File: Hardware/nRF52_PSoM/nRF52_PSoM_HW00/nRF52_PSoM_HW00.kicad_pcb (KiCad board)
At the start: 4 copper layers, 22 x 25.6 mm, 54 parts, among them J101 USB4510-03-1-A, J102 54722-0604, SW401 SW_Push, SW402 SW_Push, U201 BQ24075RGTR, U301 MIC5528-3.3YMT-T5, U401 ESP32-S2FH4, Y601 Crystal_GND24_Small

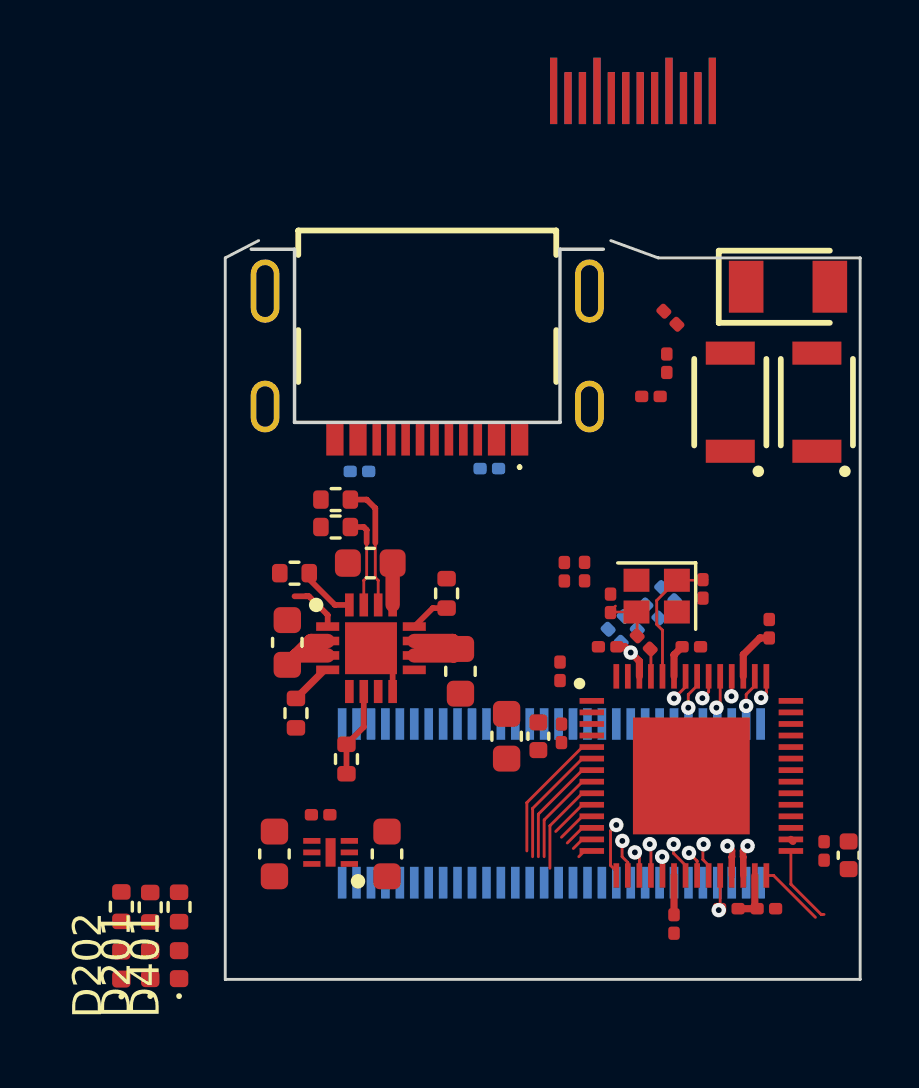
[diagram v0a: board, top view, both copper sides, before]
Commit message: Routing ESP32S2
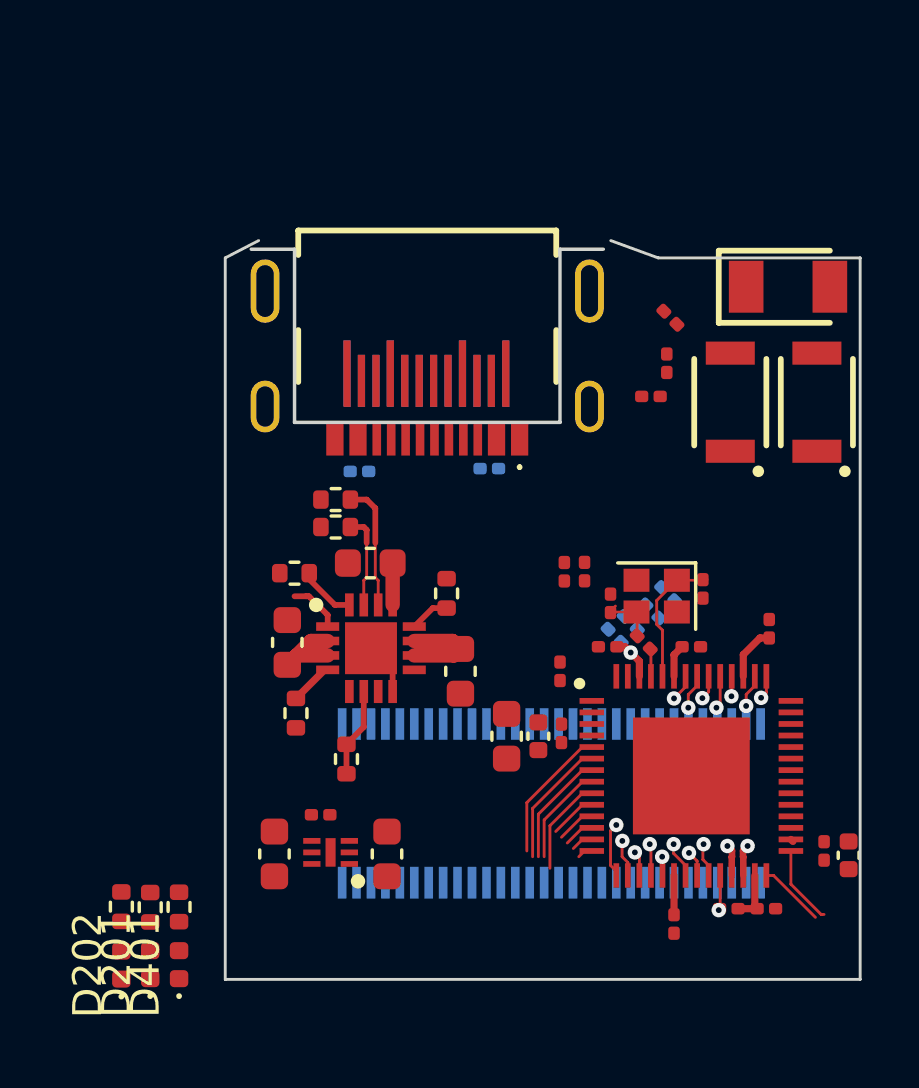
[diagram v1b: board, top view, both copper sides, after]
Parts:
- REF**: moved to F.Cu
- moved REF** 12.1 mm to (159.0, 41.9), turned to 0 degrees
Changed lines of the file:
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@@
     )
+  )
+  (footprint "Component_lib:usb-c-pcb" (layer "F.Cu")
+    (at 158.97 41.86)
+    (attr through_hole)
+    (fp_text reference "REF**" (at 6.8 3.6) (layer "F.SilkS") hide
+        (effects (font (size 1 1) (thickness 0.15)))
+    )
+    (fp_text value "usb-c-pcb" (at -0.3 -8.6) (layer "F.Fab")
+        (effects (font (size 1 1) (thickness 0.15)))
+    )
+    (fp_line (start -3.34 -3.85) (end -3.34 -3.2)
+      (stroke (width 0.05) (type solid)) (layer "Dwgs.User"))
+    (fp_line (start -3.11 -4.45) (end -3.34 -3.85)
+      (stroke (width 0.05) (type solid)) (layer "Dwgs.User"))
+    (fp_line (start -3.095 -4.45) (end 3.095 -4.45)
+      (stroke (width 0.05) (type solid)) (layer "Dwgs.User"))
+    (fp_line (start -3.04 -2.9) (end -3.04 -2)
+      (stroke (width 0.05) (type solid)) (layer "Dwgs.User"))
+    (fp_line (start -3 -1.5) (end -3 0)
+      (stroke (width 0.05) (type solid)) (layer "Dwgs.User"))
+    (fp_line (start -3 0) (end 3 0)
+      (stroke (width 0.05) (type solid)) (layer "Dwgs.User"))
+    (fp_line (start 3 -1.5) (end -3 -1.5)
+      (stroke (width 0.05) (type solid)) (layer "Dwgs.User"))
+    (fp_line (start 3 0) (end 3 -1.5)
+      (stroke (width 0.05) (type solid)) (layer "Dwgs.User"))
+    (fp_line (start 3.04 -2.9) (end 3.04 -1.99)
+      (stroke (width 0.05) (type solid)) (layer "Dwgs.User"))
+    (fp_line (start 3.1 -4.45) (end 3.35 -3.85)
+      (stroke (width 0.05) (type solid)) (layer "Dwgs.User"))
+    (fp_line (start 3.35 -3.85) (end 3.35 -3.2)
+      (stroke (width 0.05) (type solid)) (layer "Dwgs.User"))
+    (fp_arc (start -3.34 -3.2) (mid -3.127868 -3.112132) (end -3.04 -2.9)
+      (stroke (width 0.05) (type solid)) (layer "Dwgs.User"))
+    (fp_arc (start -3.04 -2) (mid -3.127868 -1.787868) (end -3.34 -1.7)
+      (stroke (width 0.05) (type solid)) (layer "Dwgs.User"))
+    (fp_arc (start -3.02 -1.38) (mid -3.246274 -1.473726) (end -3.34 -1.7)
+      (stroke (width 0.05) (type solid)) (layer "Dwgs.User"))
+    (fp_arc (start 3.039833 -2.900048) (mid 3.131333 -3.115773) (end 3.35 -3.2)
+      (stroke (width 0.05) (type solid)) (layer "Dwgs.User"))
+    (fp_arc (start 3.34 -1.7) (mid 3.246274 -1.473726) (end 3.02 -1.38)
+      (stroke (width 0.05) (type solid)) (layer "Dwgs.User"))
+    (fp_arc (start 3.34 -1.7) (mid 3.127868 -1.787868) (end 3.04 -2)
+      (stroke (width 0.05) (type solid)) (layer "Dwgs.User"))
+    (pad "A1" smd rect (at 2.75 -2.85) (size 0.25 2.3) (layers "F.Cu" "F.Paste" "F.Mask"))
+    (pad "A2" smd rect (at 2.25 -2.6) (size 0.25 1.8) (layers "F.Cu" "F.Paste" "F.Mask"))
+    (pad "A3" smd rect (at 1.75 -2.6) (size 0.25 1.8) (layers "F.Cu" "F.Paste" "F.Mask"))
+    (pad "A4" smd rect (at 1.25 -2.85) (size 0.25 2.3) (layers "F.Cu" "F.Paste" "F.Mask"))
+    (pad "A5" smd rect (at 0.75 -2.6) (size 0.25 1.8) (layers "F.Cu" "F.Paste" "F.Mask"))
+    (pad "A6" smd rect (at 0.25 -2.6) (size 0.25 1.8) (layers "F.Cu" "F.Paste" "F.Mask"))
+    (pad "A7" smd rect (at -0.25 -2.6) (size 0.25 1.8) (layers "F.Cu" "F.Paste" "F.Mask"))
+    (pad "A8" smd rect (at -0.75 -2.6) (size 0.25 1.8) (layers "F.Cu" "F.Paste" "F.Mask"))
+    (pad "A9" smd rect (at -1.25 -2.85) (size 0.25 2.3) (layers "F.Cu" "F.Paste" "F.Mask"))
+    (pad "A10" smd rect (at -1.75 -2.6) (size 0.25 1.8) (layers "F.Cu" "F.Paste" "F.Mask"))
+    (pad "A11" smd rect (at -2.25 -2.6) (size 0.25 1.8) (layers "F.Cu" "F.Paste" "F.Mask"))
+    (pad "A12" smd rect (at -2.75 -2.85) (size 0.25 2.3) (layers "F.Cu" "F.Paste" "F.Mask"))
+    (pad "B1" smd rect (at -2.75 -2.85 180) (size 0.25 2.3) (layers "B.Cu" "B.Paste" "B.Mask"))
+    (pad "B2" smd rect (at -2.25 -2.6 180) (size 0.25 1.8) (layers "B.Cu" "B.Paste" "B.Mask"))
+    (pad "B3" smd rect (at -1.75 -2.6 180) (size 0.25 1.8) (layers "B.Cu" "B.Paste" "B.Mask"))
+    (pad "B4" smd rect (at -1.25 -2.85 180) (size 0.25 2.3) (layers "B.Cu" "B.Paste" "B.Mask"))
+    (pad "B5" smd rect (at -0.75 -2.6 180) (size 0.25 1.8) (layers "B.Cu" "B.Paste" "B.Mask"))
+    (pad "B6" smd rect (at -0.25 -2.6 180) (size 0.25 1.8) (layers "B.Cu" "B.Paste" "B.Mask"))
+    (pad "B7" smd rect (at 0.25 -2.6 180) (size 0.25 1.8) (layers "B.Cu" "B.Paste" "B.Mask"))
+    (pad "B8" smd rect (at 0.75 -2.6 180) (size 0.25 1.8) (layers "B.Cu" "B.Paste" "B.Mask"))
+    (pad "B9" smd rect (at 1.25 -2.85 180) (size 0.25 2.3) (layers "B.Cu" "B.Paste" "B.Mask"))
+    (pad "B10" smd rect (at 1.75 -2.6 180) (size 0.25 1.8) (layers "B.Cu" "B.Paste" "B.Mask"))
+    (pad "B11" smd rect (at 2.25 -2.6 180) (size 0.25 1.8) (layers "B.Cu" "B.Paste" "B.Mask"))
+    (pad "B12" smd rect (at 2.75 -2.85 180) (size 0.25 2.3) (layers "B.Cu" "B.Paste" "B.Mask"))
   )
   (footprint "Resistor_SMD:R_0402_1005Metric" (layer "F.Cu")
@@
     )
   )
-  (footprint "Component_lib:usb-c-pcb" (layer "B.Cu")
-    (at 166.128 32.064 180)
-    (attr through_hole)
-    (fp_text reference "REF**" (at 6.8 -3.6) (layer "B.SilkS") hide
-        (effects (font (size 1 1) (thickness 0.15)) (justify mirror))
-    )
-    (fp_text value "usb-c-pcb" (at -0.3 8.6) (layer "B.Fab")
-        (effects (font (size 1 1) (thickness 0.15)) (justify mirror))
-    )
-    (fp_line (start -3.34 3.85) (end -3.34 3.2)
-      (stroke (width 0.05) (type solid)) (layer "Dwgs.User"))
-    (fp_line (start -3.11 4.45) (end -3.34 3.85)
-      (stroke (width 0.05) (type solid)) (layer "Dwgs.User"))
-    (fp_line (start -3.095 4.45) (end 3.095 4.45)
-      (stroke (width 0.05) (type solid)) (layer "Dwgs.User"))
-    (fp_line (start -3.04 2.9) (end -3.04 2)
-      (stroke (width 0.05) (type solid)) (layer "Dwgs.User"))
-    (fp_line (start -3 0) (end 3 0)
-      (stroke (width 0.05) (type solid)) (layer "Dwgs.User"))
-    (fp_line (start -3 1.5) (end -3 0)
-      (stroke (width 0.05) (type solid)) (layer "Dwgs.User"))
-    (fp_line (start 3 0) (end 3 1.5)
-      (stroke (width 0.05) (type solid)) (layer "Dwgs.User"))
-    (fp_line (start 3 1.5) (end -3 1.5)
-      (stroke (width 0.05) (type solid)) (layer "Dwgs.User"))
-    (fp_line (start 3.04 2.9) (end 3.04 1.99)
-      (stroke (width 0.05) (type solid)) (layer "Dwgs.User"))
-    (fp_line (start 3.1 4.45) (end 3.35 3.85)
-      (stroke (width 0.05) (type solid)) (layer "Dwgs.User"))
-    (fp_line (start 3.35 3.85) (end 3.35 3.2)
-      (stroke (width 0.05) (type solid)) (layer "Dwgs.User"))
-    (fp_arc (start -3.34 1.7) (mid -3.127868 1.787868) (end -3.04 2)
-      (stroke (width 0.05) (type solid)) (layer "Dwgs.User"))
-    (fp_arc (start -3.34 1.7) (mid -3.246274 1.473726) (end -3.02 1.38)
-      (stroke (width 0.05) (type solid)) (layer "Dwgs.User"))
-    (fp_arc (start -3.04 2.9) (mid -3.127868 3.112132) (end -3.34 3.2)
-      (stroke (width 0.05) (type solid)) (layer "Dwgs.User"))
-    (fp_arc (start 3.02 1.38) (mid 3.246274 1.473726) (end 3.34 1.7)
-      (stroke (width 0.05) (type solid)) (layer "Dwgs.User"))
-    (fp_arc (start 3.04 2) (mid 3.127868 1.787868) (end 3.34 1.7)
-      (stroke (width 0.05) (type solid)) (layer "Dwgs.User"))
-    (fp_arc (start 3.35 3.2) (mid 3.131333 3.115773) (end 3.039833 2.900048)
-      (stroke (width 0.05) (type solid)) (layer "Dwgs.User"))
-    (pad "A1" smd rect (at 2.75 2.85 180) (size 0.25 2.3) (layers "B.Cu" "B.Paste" "B.Mask"))
-    (pad "A2" smd rect (at 2.25 2.6 180) (size 0.25 1.8) (layers "B.Cu" "B.Paste" "B.Mask"))
-    (pad "A3" smd rect (at 1.75 2.6 180) (size 0.25 1.8) (layers "B.Cu" "B.Paste" "B.Mask"))
-    (pad "A4" smd rect (at 1.25 2.85 180) (size 0.25 2.3) (layers "B.Cu" "B.Paste" "B.Mask"))
-    (pad "A5" smd rect (at 0.75 2.6 180) (size 0.25 1.8) (layers "B.Cu" "B.Paste" "B.Mask"))
-    (pad "A6" smd rect (at 0.25 2.6 180) (size 0.25 1.8) (layers "B.Cu" "B.Paste" "B.Mask"))
-    (pad "A7" smd rect (at -0.25 2.6 180) (size 0.25 1.8) (layers "B.Cu" "B.Paste" "B.Mask"))
-    (pad "A8" smd rect (at -0.75 2.6 180) (size 0.25 1.8) (layers "B.Cu" "B.Paste" "B.Mask"))
-    (pad "A9" smd rect (at -1.25 2.85 180) (size 0.25 2.3) (layers "B.Cu" "B.Paste" "B.Mask"))
-    (pad "A10" smd rect (at -1.75 2.6 180) (size 0.25 1.8) (layers "B.Cu" "B.Paste" "B.Mask"))
-    (pad "A11" smd rect (at -2.25 2.6 180) (size 0.25 1.8) (layers "B.Cu" "B.Paste" "B.Mask"))
-    (pad "A12" smd rect (at -2.75 2.85 180) (size 0.25 2.3) (layers "B.Cu" "B.Paste" "B.Mask"))
-    (pad "B1" smd rect (at -2.75 2.85) (size 0.25 2.3) (layers "F.Cu" "F.Paste" "F.Mask"))
-    (pad "B2" smd rect (at -2.25 2.6) (size 0.25 1.8) (layers "F.Cu" "F.Paste" "F.Mask"))
-    (pad "B3" smd rect (at -1.75 2.6) (size 0.25 1.8) (layers "F.Cu" "F.Paste" "F.Mask"))
-    (pad "B4" smd rect (at -1.25 2.85) (size 0.25 2.3) (layers "F.Cu" "F.Paste" "F.Mask"))
-    (pad "B5" smd rect (at -0.75 2.6) (size 0.25 1.8) (layers "F.Cu" "F.Paste" "F.Mask"))
-    (pad "B6" smd rect (at -0.25 2.6) (size 0.25 1.8) (layers "F.Cu" "F.Paste" "F.Mask"))
-    (pad "B7" smd rect (at 0.25 2.6) (size 0.25 1.8) (layers "F.Cu" "F.Paste" "F.Mask"))
-    (pad "B8" smd rect (at 0.75 2.6) (size 0.25 1.8) (layers "F.Cu" "F.Paste" "F.Mask"))
-    (pad "B9" smd rect (at 1.25 2.85) (size 0.25 2.3) (layers "F.Cu" "F.Paste" "F.Mask"))
-    (pad "B10" smd rect (at 1.75 2.6) (size 0.25 1.8) (layers "F.Cu" "F.Paste" "F.Mask"))
-    (pad "B11" smd rect (at 2.25 2.6) (size 0.25 1.8) (layers "F.Cu" "F.Paste" "F.Mask"))
-    (pad "B12" smd rect (at 2.75 2.85) (size 0.25 2.3) (layers "F.Cu" "F.Paste" "F.Mask"))
-  )
   (footprint "Resistor_SMD:R_0201_0603Metric" (layer "B.Cu")
